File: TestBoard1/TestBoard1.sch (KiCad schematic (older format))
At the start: 2 parts

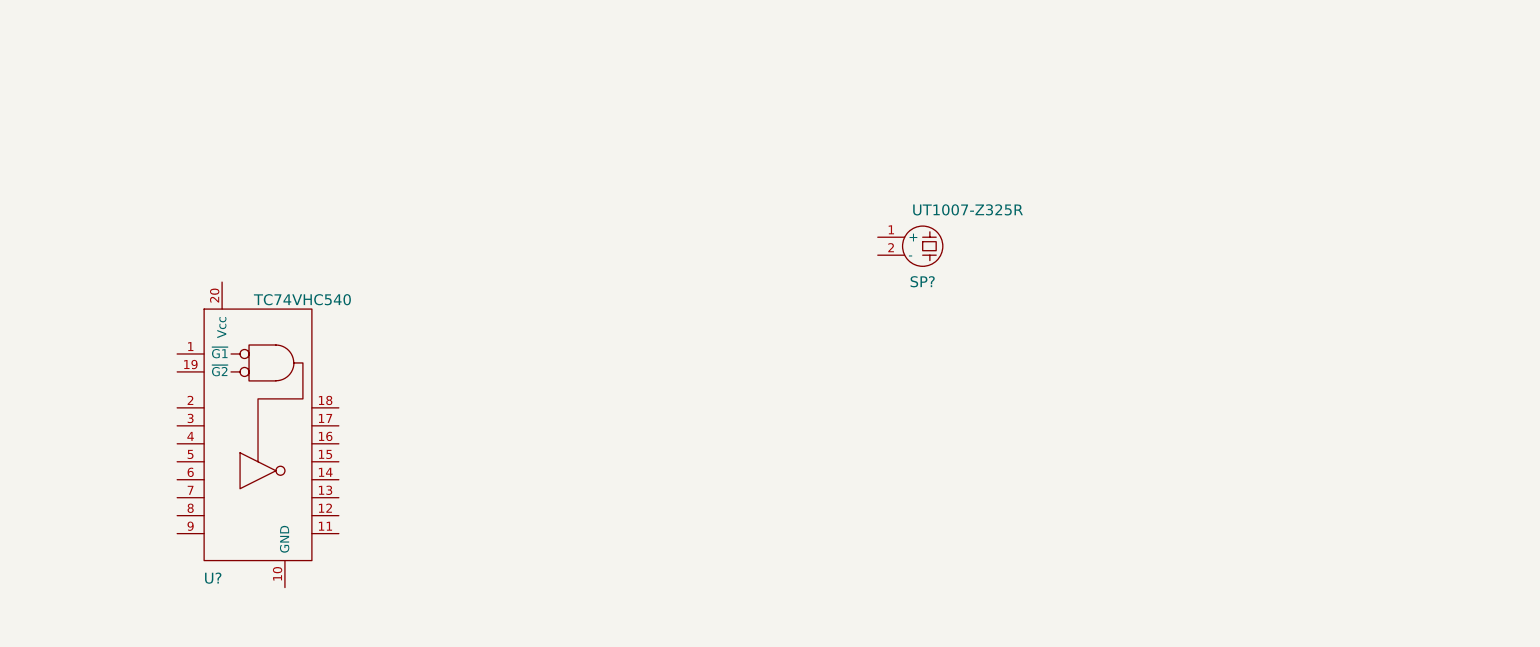
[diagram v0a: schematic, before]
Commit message: 超音波送受信テストボードを追加
PCBGOGOに基板を発注
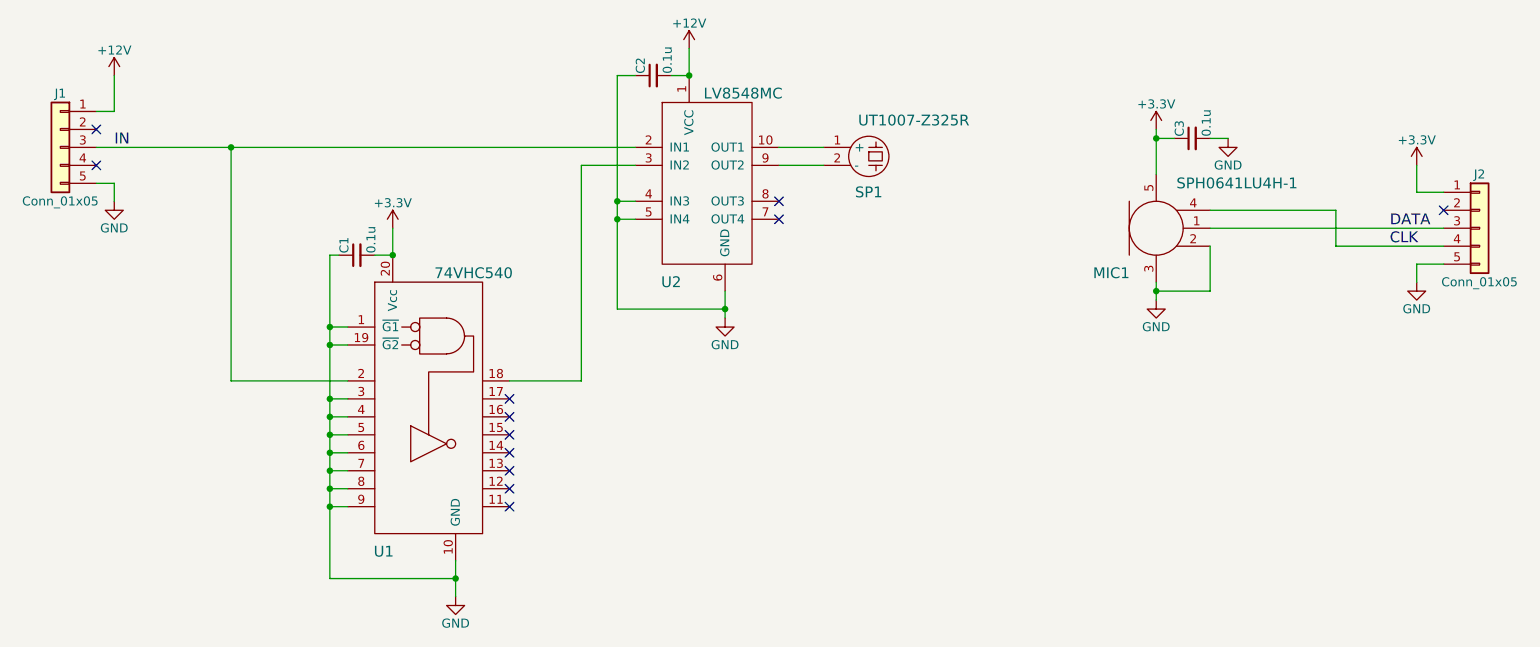
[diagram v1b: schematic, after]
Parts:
- added C1, C2, C3: 0.1u, Capacitors_SMD:C_0603_HandSoldering, symbol C_Small
- added J1, J2: Conn_01x05, Pin_Headers:Pin_Header_Straight_1x05_Pitch2.54mm, symbol Conn_01x05
- added MIC1: SPH0641LU4H-1, KiCad_Footprints:SPH0641LU4H-1, symbol SPH0641LU4H-1
- added U2: LV8548MC, KiCad_Footprints:SOIC10, symbol LV8548MC
- SP1: renamed from SP?; footprint (none) -> KiCad_Footprints:UT1007-Z325R
- U1: renamed from U?; value TC74VHC540 -> 74VHC540; footprint (none) -> KiCad_Footprints:SSOP20
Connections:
- net GND: now reaches U1.1 (~G1)
- net GND: now also U1.10 (GND), U1.19 (~G2), U1.3, U1.4, U1.5, U1.6, U1.7, U1.8, U1.9, C1.1, C2.1, C3.2, J1.5 (Pin_5), J2.5 (Pin_5), MIC1.2 (SELECT), MIC1.3 (GND), U2.4 (IN3), U2.5 (IN4), U2.6 (GND)
- net at U1.18: now also U2.3 (IN2)
- net IN: now reaches U1.2
- net IN: now also J1.3 (Pin_3), U2.2 (IN1)
- net +3V3: now reaches U1.20 (Vcc)
- net +3V3: now also C1.2, C3.1, J2.1 (Pin_1), MIC1.5 (VDD)
- net at SP1.1 (+): now also U2.10 (OUT1)
- net at SP1.2 (-): now also U2.9 (OUT2)
- new net +12V: C2.2, J1.1 (Pin_1), U2.1 (VCC)
- new net CLK: J2.4 (Pin_4), MIC1.4 (CLOCK)
- new net DATA: J2.3 (Pin_3), MIC1.1 (DATA)
- no-connect marks 0 -> 12
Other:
- moved on the sheet: SP1, U1
